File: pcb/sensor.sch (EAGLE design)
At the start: 14 parts, among them IC2 4512N, Q1 BUZ10, U1 ARDUINOR3-DIMENSION

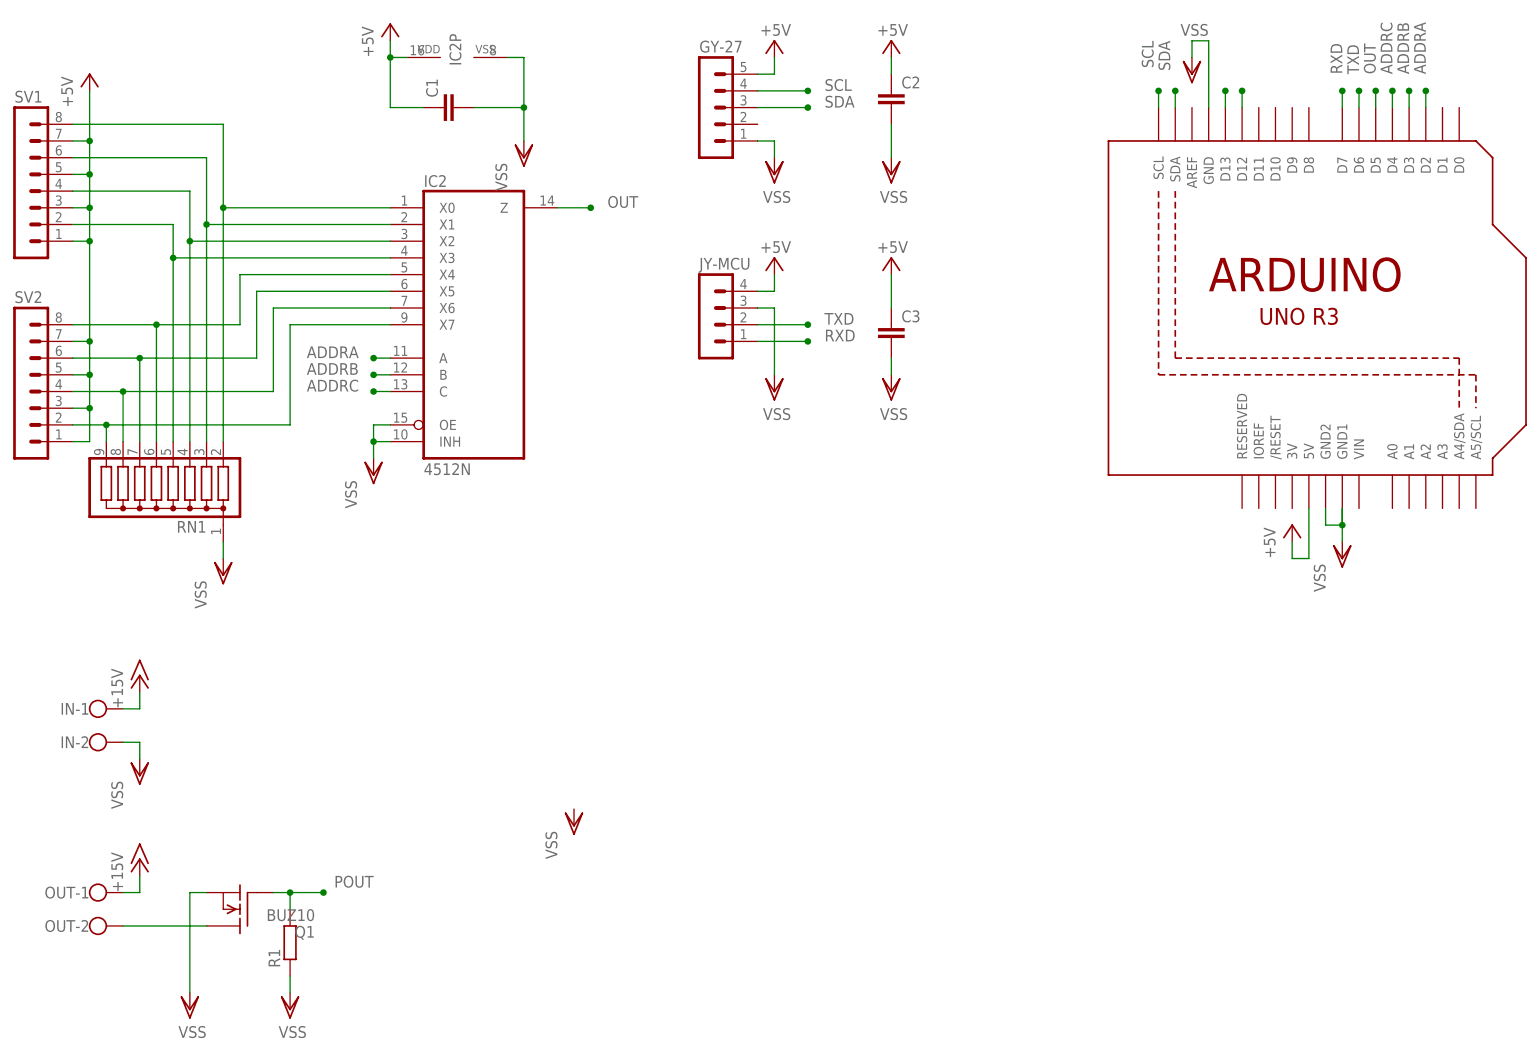
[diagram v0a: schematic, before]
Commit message: Added led strip connector
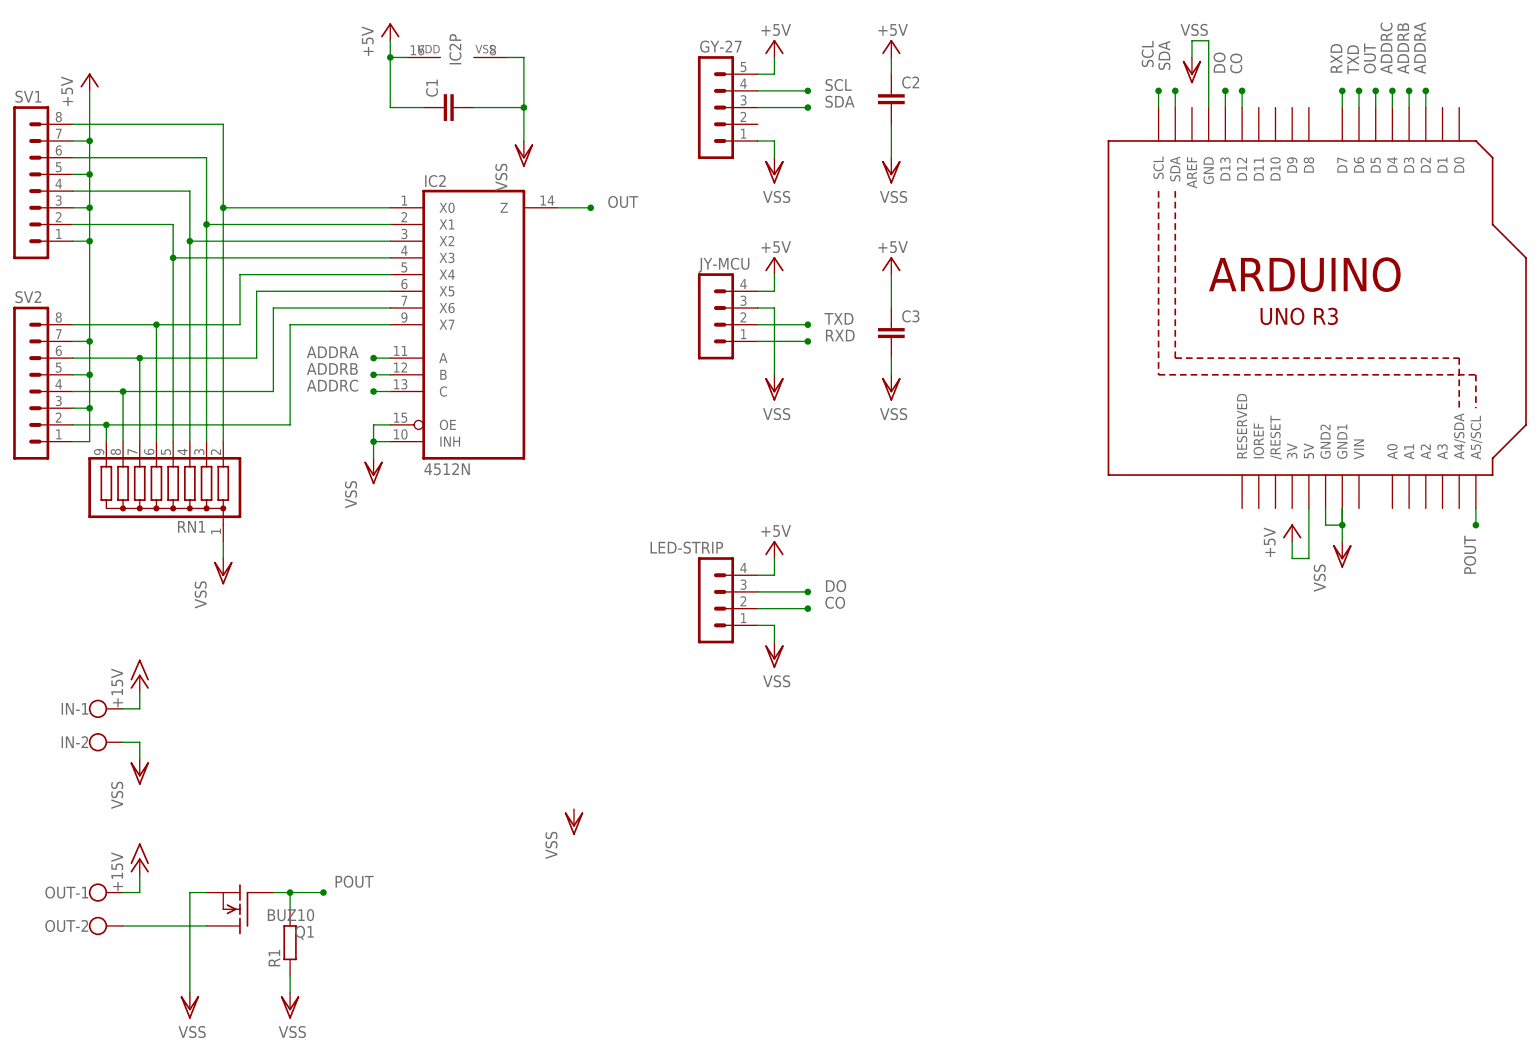
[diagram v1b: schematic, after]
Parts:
- added LED-STRIP: (no value), con-lstb:MA04-1
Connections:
- removed net N$8: U1.D13
- new net CO: LED-STRIP.2, U1.D12
- new net DO: LED-STRIP.3, U1.D13
- net +5V: now also LED-STRIP.4
- net POUT: now also U1.A5/SCL; no longer U1.D12
- net VSS: now also LED-STRIP.1
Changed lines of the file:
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@@
 <part name="IC2" library="45xx" deviceset="4512" device="N"/>
 <part name="Q1" library="transistor-fet" deviceset="BUZ10" device=""/>
+<part name="LED-STRIP" library="con-lstb" deviceset="MA04-1" device=""/>
+<part name="P+10" library="supply1" deviceset="+5V" device=""/>
+<part name="VSS14" library="supply1" deviceset="VSS" device=""/>
 </parts>
 <sheets>
@@
 <instance part="IC2" gate="P" x="83.82" y="162.56" rot="R90"/>
 <instance part="Q1" gate="G$1" x="50.8" y="33.02" rot="R180"/>
+<instance part="LED-STRIP" gate="1" x="121.92" y="81.28" smashed="yes">
+<attribute name="VALUE" x="120.65" y="71.12" size="1.778" layer="96"/>
+<attribute name="NAME" x="113.03" y="87.122" size="1.778" layer="95"/>
+</instance>
+<instance part="P+10" gate="1" x="132.08" y="88.9" smashed="yes">
+<attribute name="VALUE" x="134.62" y="91.44" size="1.778" layer="96" rot="R180"/>
+</instance>
+<instance part="VSS14" gate="G$1" x="132.08" y="71.12" smashed="yes">
+<attribute name="VALUE" x="134.62" y="68.58" size="1.778" layer="96" rot="R180"/>
+</instance>
 </instances>
 <busses>
@@
 <wire x1="149.86" y1="129.54" x2="149.86" y2="124.46" width="0.1524" layer="91"/>
 </segment>
+<segment>
+<pinref part="LED-STRIP" gate="1" pin="4"/>
+<wire x1="129.54" y1="83.82" x2="132.08" y2="83.82" width="0.1524" layer="91"/>
+<pinref part="P+10" gate="1" pin="+5V"/>
+<wire x1="132.08" y1="83.82" x2="132.08" y2="86.36" width="0.1524" layer="91"/>
+</segment>
 </net>
 <net name="VSS" class="0">
@@
 <wire x1="35.56" y1="58.42" x2="35.56" y2="55.88" width="0.1524" layer="91"/>
 </segment>
+<segment>
+<pinref part="LED-STRIP" gate="1" pin="1"/>
+<wire x1="129.54" y1="76.2" x2="132.08" y2="76.2" width="0.1524" layer="91"/>
+<pinref part="VSS14" gate="G$1" pin="VSS"/>
+<wire x1="132.08" y1="76.2" x2="132.08" y2="73.66" width="0.1524" layer="91"/>
+</segment>
 </net>
 <net name="N$4" class="0">
@@
 </segment>
 </net>
-<net name="N$8" class="0">
-<segment>
-<pinref part="U1" gate="G$1" pin="D13"/>
-<wire x1="200.66" y1="154.94" x2="200.66" y2="157.48" width="0.1524" layer="91"/>
-<junction x="200.66" y="157.48"/>
-</segment>
-</net>
 <net name="SDA" class="0">
 <segment>
@@
 </segment>
 <segment>
-<pinref part="U1" gate="G$1" pin="D12"/>
-<wire x1="203.2" y1="154.94" x2="203.2" y2="157.48" width="0.1524" layer="91"/>
-<junction x="203.2" y="157.48"/>
+<pinref part="U1" gate="G$1" pin="A5/SCL"/>
+<wire x1="238.76" y1="93.98" x2="238.76" y2="91.44" width="0.1524" layer="91"/>
+<junction x="238.76" y="91.44"/>
+<label x="238.76" y="83.82" size="1.778" layer="95" rot="R90"/>
 </segment>
 </net>
@@
 </segment>
 </net>
+<net name="CO" class="0">
+<segment>
+<pinref part="LED-STRIP" gate="1" pin="2"/>
+<wire x1="129.54" y1="78.74" x2="137.16" y2="78.74" width="0.1524" layer="91"/>
+<junction x="137.16" y="78.74"/>
+<label x="139.7" y="78.74" size="1.778" layer="95"/>
+</segment>
+<segment>
+<pinref part="U1" gate="G$1" pin="D12"/>
+<wire x1="203.2" y1="154.94" x2="203.2" y2="157.48" width="0.1524" layer="91"/>
+<junction x="203.2" y="157.48"/>
+<label x="203.2" y="160.02" size="1.778" layer="95" rot="R90"/>
+</segment>
+</net>
+<net name="DO" class="0">
+<segment>
+<pinref part="LED-STRIP" gate="1" pin="3"/>
+<wire x1="129.54" y1="81.28" x2="137.16" y2="81.28" width="0.1524" layer="91"/>
+<junction x="137.16" y="81.28"/>
+<label x="139.7" y="81.28" size="1.778" layer="95"/>
+</segment>
+<segment>
+<pinref part="U1" gate="G$1" pin="D13"/>
+<wire x1="200.66" y1="154.94" x2="200.66" y2="157.48" width="0.1524" layer="91"/>
+<junction x="200.66" y="157.48"/>
+<label x="200.66" y="160.02" size="1.778" layer="95" rot="R90"/>
+</segment>
+</net>
